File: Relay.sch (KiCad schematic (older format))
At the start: 0 parts

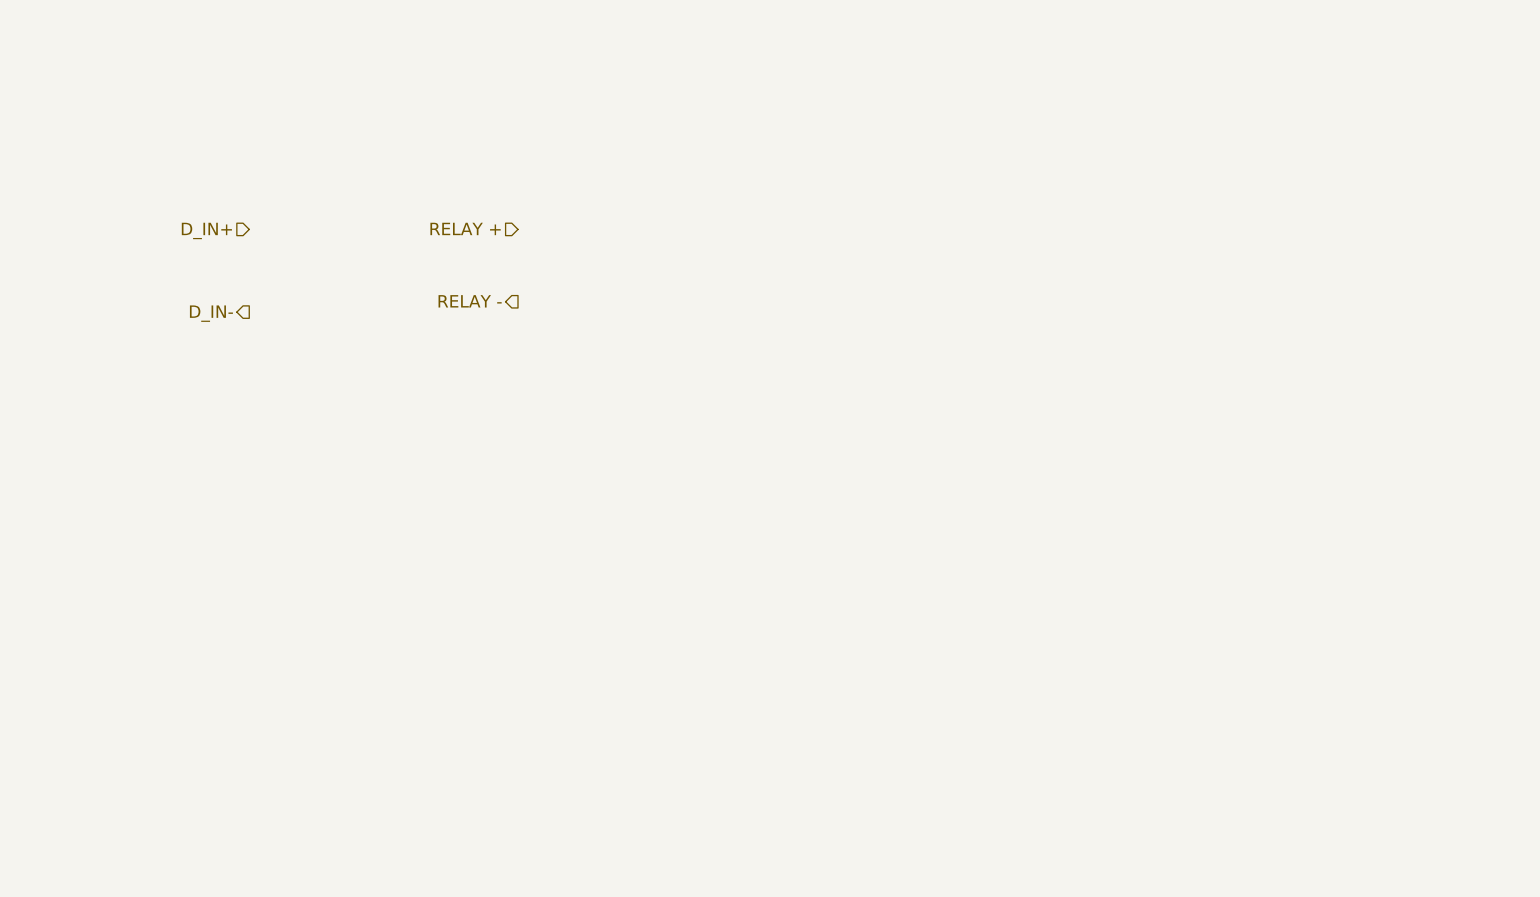
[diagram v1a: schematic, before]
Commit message: Added Relay and Fan subsystem block diagrams
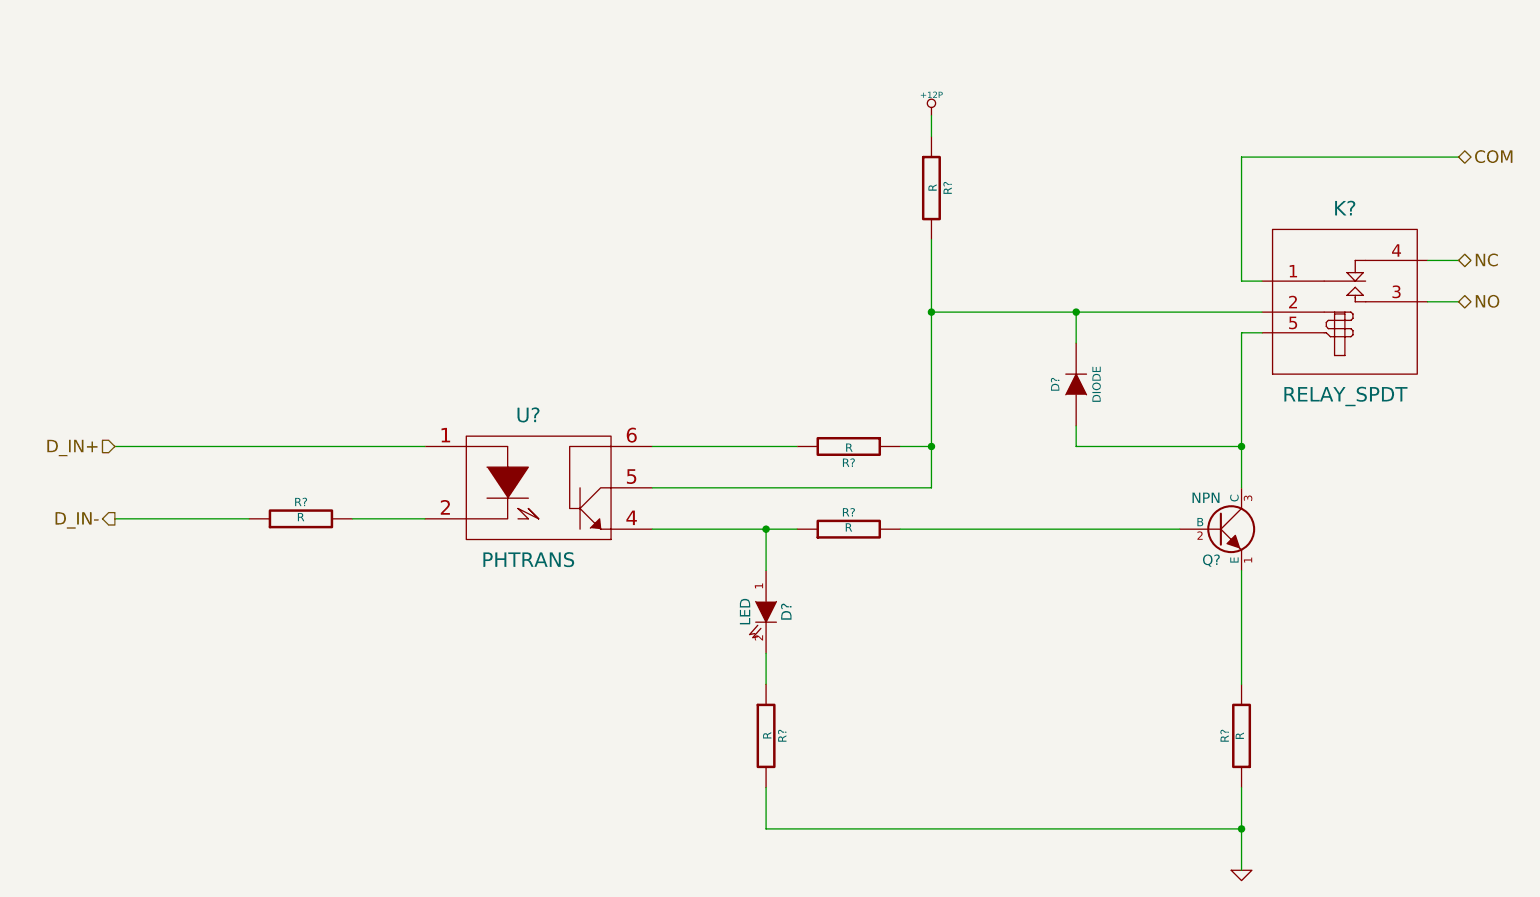
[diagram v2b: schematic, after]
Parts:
- added D?: LED, ~, symbol LED
- added D?: DIODE, ~, symbol DIODE
- added K?: RELAY_SPDT, ~, symbol RELAY_SPDT
- added Q?: NPN, ~, symbol NPN
- added R? (x6): R, ~, symbol R
- added U?: PHTRANS, ~, symbol PHTRANS
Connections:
- net D_IN+: now also U?.1
- net D_IN-: now also R?.1
- new net: R?.2, U?.2
- new net: D?.1 (A), R?.1, U?.4
- new net: D?.2 (K), K?.2 (COIL+), R?.1, R?.2, U?.5
- new net: R?.2, U?.6
- new net: Q?.1 (E), R?.2
- new net: Q?.2 (B), R?.2
- new net: D?.1 (A), K?.5 (COIL-), Q?.3 (C)
- new net: D?.2 (K), R?.1
- new net +12P: R?.1
- new net COM: K?.1 (COM)
- new net GND: R?.1, R?.2
- new net NC: K?.4 (NC)
- new net NO: K?.3 (NO)
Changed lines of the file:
@@
 LIBS:contrib
 LIBS:valves
+LIBS:CE_BenchBuddEE
 LIBS:CE_BenchBuddEE-cache
 EELAYER 27 0
@@
 $Descr A4 11693 8268
 encoding utf-8
-Sheet 7 8
+Sheet 6 8
 Title ""
-Date "4 feb 2014"
+Date "5 feb 2014"
 Rev ""
 Comp ""
@@
 Comment4 ""
 $EndDescr
-Text HLabel 3000 2650 0    60   Input ~ 0
+Text HLabel 2350 3700 0    60   Input ~ 0
 D_IN+
-Text HLabel 3000 3050 0    60   Output ~ 0
+Text HLabel 2350 4050 0    60   Output ~ 0
 D_IN-
-Text HLabel 4300 2650 0    60   Input ~ 0
-RELAY +
-Text HLabel 4300 3000 0    60   Output ~ 0
-RELAY -
+Text HLabel 8850 2800 2    60   BiDi ~ 0
+NC
+Text HLabel 8850 3000 2    60   BiDi ~ 0
+NO
+$Comp
+L PHTRANS U?
+U 1 1 52F2AFC1
+P 4400 3900
+F 0 "U?" H 4350 4250 70  0000 C CNN
+F 1 "PHTRANS" H 4350 3550 70  0000 C CNN
+F 2 "~" H 4400 3900 60  0000 C CNN
+F 3 "~" H 4400 3900 60  0000 C CNN
+	1    4400 3900
+	1    0    0    -1
+$EndComp
+$Comp
+L R R?
+U 1 1 52F2AFD0
+P 6300 2450
+F 0 "R?" V 6380 2450 40  0000 C CNN
+F 1 "R" V 6307 2451 40  0000 C CNN
+F 2 "~" V 6230 2450 30  0000 C CNN
+F 3 "~" H 6300 2450 30  0000 C CNN
+	1    6300 2450
+	1    0    0    -1
+$EndComp
+$Comp
+L NPN Q?
+U 1 1 52F2AFDF
+P 7700 4100
+F 0 "Q?" H 7700 3950 50  0000 R CNN
+F 1 "NPN" H 7700 4250 50  0000 R CNN
+F 2 "~" H 7700 4100 60  0000 C CNN
+F 3 "~" H 7700 4100 60  0000 C CNN
+	1    7700 4100
+	1    0    0    -1
+$EndComp
+$Comp
+L LED D?
+U 1 1 52F2AFEE
+P 5500 4500
+F 0 "D?" H 5500 4600 50  0000 C CNN
+F 1 "LED" H 5500 4400 50  0000 C CNN
+F 2 "~" H 5500 4500 60  0000 C CNN
+F 3 "~" H 5500 4500 60  0000 C CNN
+	1    5500 4500
+	0    1    1    0
+$EndComp
+$Comp
+L RELAY_SPDT K?
+U 1 1 52F2C7E8
+P 8300 3000
+F 0 "K?" H 8300 3450 70  0000 C CNN
+F 1 "RELAY_SPDT" H 8300 2550 70  0000 C CNN
+F 2 "~" H 8300 3000 60  0000 C CNN
+F 3 "~" H 8300 3000 60  0000 C CNN
+	1    8300 3000
+	1    0    0    -1
+$EndComp
+Text HLabel 8850 2300 2    60   BiDi ~ 0
+COM
+Wire Wire Line
+	8850 2800 8700 2800
+Wire Wire Line
+	8850 3000 8700 3000
+$Comp
+L R R?
+U 1 1 52F2C854
+P 5900 4100
+F 0 "R?" V 5980 4100 40  0000 C CNN
+F 1 "R" V 5907 4101 40  0000 C CNN
+F 2 "~" V 5830 4100 30  0000 C CNN
+F 3 "~" H 5900 4100 30  0000 C CNN
+	1    5900 4100
+	0    -1   -1   0
+$EndComp
+Wire Wire Line
+	4950 4100 5500 4100
+Wire Wire Line
+	5500 4100 5650 4100
+Wire Wire Line
+	6150 4100 7500 4100
+$Comp
+L R R?
+U 1 1 52F2C889
+P 7800 5100
+F 0 "R?" V 7880 5100 40  0000 C CNN
+F 1 "R" V 7807 5101 40  0000 C CNN
+F 2 "~" V 7730 5100 30  0000 C CNN
+F 3 "~" H 7800 5100 30  0000 C CNN
+	1    7800 5100
+	-1   0    0    1
+$EndComp
+Wire Wire Line
+	7800 4300 7800 4850
+$Comp
+L GND #PWR?
+U 1 1 52F2C8A3
+P 7800 5750
+F 0 "#PWR?" H 7800 5750 30  0001 C CNN
+F 1 "GND" H 7800 5680 30  0001 C CNN
+F 2 "" H 7800 5750 60  0000 C CNN
+F 3 "" H 7800 5750 60  0000 C CNN
+	1    7800 5750
+	1    0    0    -1
+$EndComp
+Wire Wire Line
+	5500 4100 5500 4300
+Connection ~ 5500 4100
+$Comp
+L R R?
+U 1 1 52F2C8D7
+P 5500 5100
+F 0 "R?" V 5580 5100 40  0000 C CNN
+F 1 "R" V 5507 5101 40  0000 C CNN
+F 2 "~" V 5430 5100 30  0000 C CNN
+F 3 "~" H 5500 5100 30  0000 C CNN
+	1    5500 5100
+	1    0    0    -1
+$EndComp
+Wire Wire Line
+	5500 4700 5500 4850
+Wire Wire Line
+	6300 2700 6300 3050
+Wire Wire Line
+	6300 3050 6300 3700
+Wire Wire Line
+	6300 3700 6300 3900
+$Comp
+L +12P #PWR?
+U 1 1 52F2C90E
+P 6300 2100
+F 0 "#PWR?" H 6300 2070 30  0001 C CNN
+F 1 "+12P" H 6300 2200 30  0000 C CNN
+F 2 "" H 6300 2100 60  0000 C CNN
+F 3 "" H 6300 2100 60  0000 C CNN
+	1    6300 2100
+	1    0    0    -1
+$EndComp
+Wire Wire Line
+	6300 2200 6300 2100
+Wire Wire Line
+	5500 5350 5500 5550
+Wire Wire Line
+	5500 5550 7800 5550
+$Comp
+L R R?
+U 1 1 52F2C93C
+P 3250 4050
+F 0 "R?" V 3330 4050 40  0000 C CNN
+F 1 "R" V 3257 4051 40  0000 C CNN
+F 2 "~" V 3180 4050 30  0000 C CNN
+F 3 "~" H 3250 4050 30  0000 C CNN
+	1    3250 4050
+	0    -1   -1   0
+$EndComp
+Wire Wire Line
+	3500 4050 3850 4050
+Wire Wire Line
+	3000 4050 2350 4050
+Wire Wire Line
+	2350 3700 3850 3700
+Wire Wire Line
+	6300 3900 4950 3900
+$Comp
+L R R?
+U 1 1 52F2C9AE
+P 5900 3700
+F 0 "R?" V 5980 3700 40  0000 C CNN
+F 1 "R" V 5907 3701 40  0000 C CNN
+F 2 "~" V 5830 3700 30  0000 C CNN
+F 3 "~" H 5900 3700 30  0000 C CNN
+	1    5900 3700
+	0    1    1    0
+$EndComp
+Wire Wire Line
+	4950 3700 5650 3700
+Wire Wire Line
+	6150 3700 6300 3700
+Connection ~ 6300 3700
+Wire Wire Line
+	7900 2900 7800 2900
+Wire Wire Line
+	7800 2900 7800 2300
+Wire Wire Line
+	7800 2300 8850 2300
+Wire Wire Line
+	6300 3050 7000 3050
+Wire Wire Line
+	7000 3050 7900 3050
+Connection ~ 6300 3050
+Wire Wire Line
+	7800 3150 7800 3700
+Wire Wire Line
+	7800 3700 7800 3900
+Wire Wire Line
+	7800 3150 7900 3150
+$Comp
+L DIODE D?
+U 1 1 52F2CA74
+P 7000 3400
+F 0 "D?" H 7000 3500 40  0000 C CNN
+F 1 "DIODE" H 7000 3300 40  0000 C CNN
+F 2 "~" H 7000 3400 60  0000 C CNN
+F 3 "~" H 7000 3400 60  0000 C CNN
+	1    7000 3400
+	0    -1   -1   0
+$EndComp
+Wire Wire Line
+	7800 3700 7000 3700
+Wire Wire Line
+	7000 3700 7000 3600
+Connection ~ 7800 3700
+Wire Wire Line
+	7000 3200 7000 3050
+Connection ~ 7000 3050
+Wire Wire Line
+	7800 5350 7800 5550
+Wire Wire Line
+	7800 5550 7800 5750
+Connection ~ 7800 5550
 $EndSCHEMATC

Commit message: Blocked out the LED Driver and Power sheets
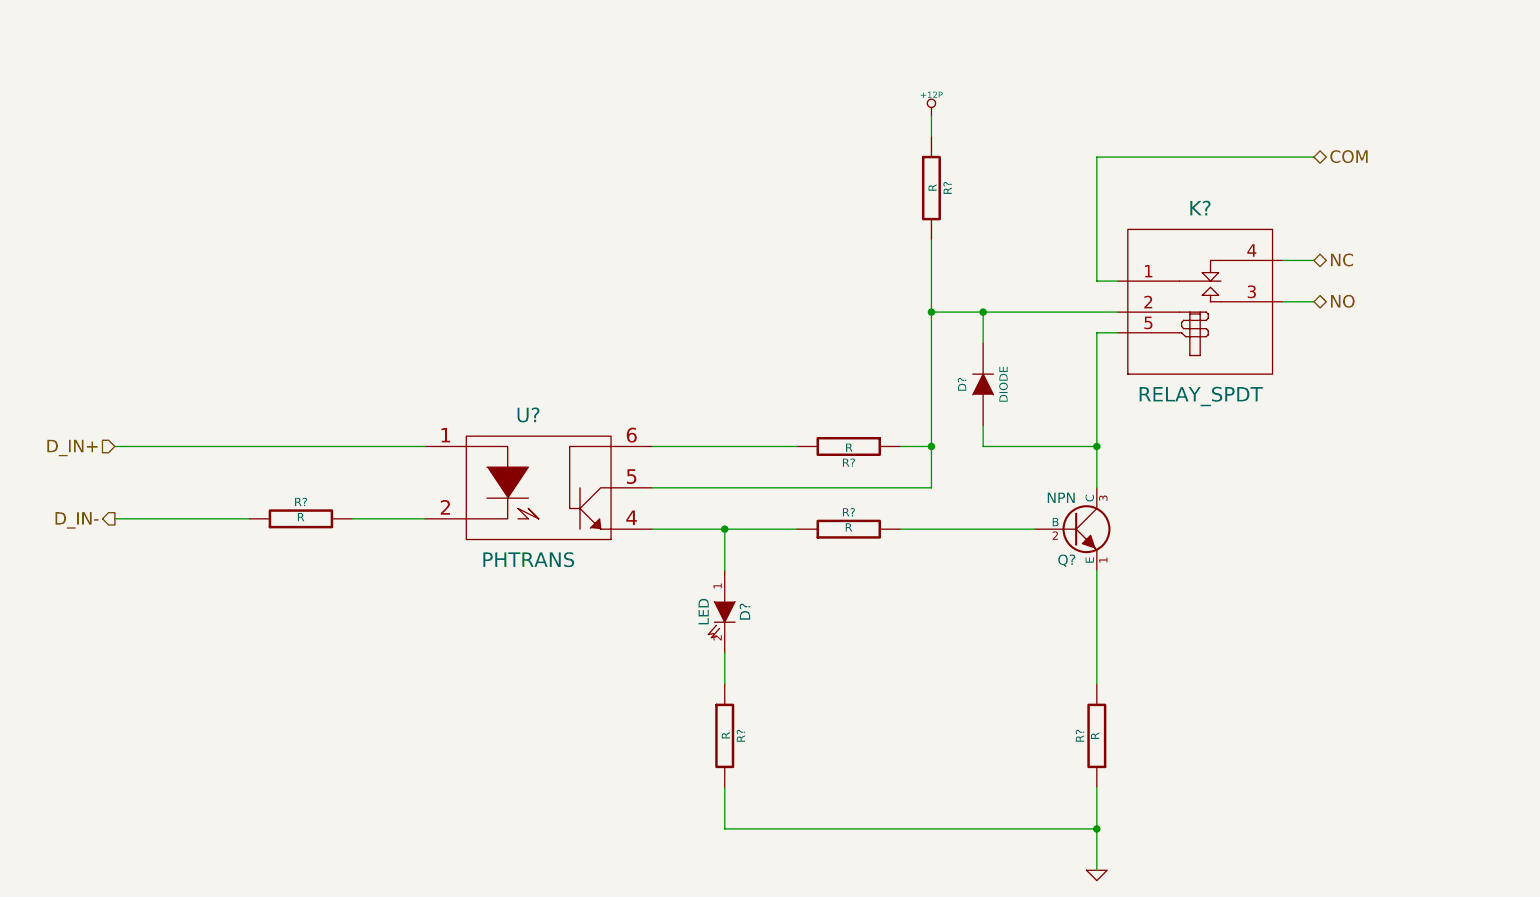
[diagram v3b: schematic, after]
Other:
- moved on the sheet: D?, K?, Q?, R?
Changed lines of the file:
@@
 LIBS:contrib
 LIBS:valves
+LIBS:CE_BenchBuddEE-cache
 LIBS:CE_BenchBuddEE
 LIBS:CE_BenchBuddEE-cache
@@
 $Descr A4 11693 8268
 encoding utf-8
-Sheet 6 8
+Sheet 4 9
 Title ""
-Date "5 feb 2014"
+Date "6 feb 2014"
 Rev ""
 Comp ""
@@
 Text HLabel 2350 4050 0    60   Output ~ 0
 D_IN-
-Text HLabel 8850 2800 2    60   BiDi ~ 0
+Text HLabel 8150 2800 2    60   BiDi ~ 0
 NC
-Text HLabel 8850 3000 2    60   BiDi ~ 0
+Text HLabel 8150 3000 2    60   BiDi ~ 0
 NO
 $Comp
@@
 L NPN Q?
 U 1 1 52F2AFDF
-P 7700 4100
-F 0 "Q?" H 7700 3950 50  0000 R CNN
-F 1 "NPN" H 7700 4250 50  0000 R CNN
-F 2 "~" H 7700 4100 60  0000 C CNN
-F 3 "~" H 7700 4100 60  0000 C CNN
-	1    7700 4100
+P 7000 4100
+F 0 "Q?" H 7000 3950 50  0000 R CNN
+F 1 "NPN" H 7000 4250 50  0000 R CNN
+F 2 "~" H 7000 4100 60  0000 C CNN
+F 3 "~" H 7000 4100 60  0000 C CNN
+	1    7000 4100
 	1    0    0    -1
 $EndComp
@@
 L LED D?
 U 1 1 52F2AFEE
-P 5500 4500
-F 0 "D?" H 5500 4600 50  0000 C CNN
-F 1 "LED" H 5500 4400 50  0000 C CNN
-F 2 "~" H 5500 4500 60  0000 C CNN
-F 3 "~" H 5500 4500 60  0000 C CNN
-	1    5500 4500
+P 5300 4500
+F 0 "D?" H 5300 4600 50  0000 C CNN
+F 1 "LED" H 5300 4400 50  0000 C CNN
+F 2 "~" H 5300 4500 60  0000 C CNN
+F 3 "~" H 5300 4500 60  0000 C CNN
+	1    5300 4500
 	0    1    1    0
 $EndComp
@@
 L RELAY_SPDT K?
 U 1 1 52F2C7E8
-P 8300 3000
-F 0 "K?" H 8300 3450 70  0000 C CNN
-F 1 "RELAY_SPDT" H 8300 2550 70  0000 C CNN
-F 2 "~" H 8300 3000 60  0000 C CNN
-F 3 "~" H 8300 3000 60  0000 C CNN
-	1    8300 3000
-	1    0    0    -1
-$EndComp
-Text HLabel 8850 2300 2    60   BiDi ~ 0
+P 7600 3000
+F 0 "K?" H 7600 3450 70  0000 C CNN
+F 1 "RELAY_SPDT" H 7600 2550 70  0000 C CNN
+F 2 "~" H 7600 3000 60  0000 C CNN
+F 3 "~" H 7600 3000 60  0000 C CNN
+	1    7600 3000
+	1    0    0    -1
+$EndComp
+Text HLabel 8150 2300 2    60   BiDi ~ 0
 COM
 Wire Wire Line
-	8850 2800 8700 2800
-Wire Wire Line
-	8850 3000 8700 3000
+	8150 2800 8000 2800
+Wire Wire Line
+	8150 3000 8000 3000
 $Comp
 L R R?
@@
 $EndComp
 Wire Wire Line
-	4950 4100 5500 4100
-Wire Wire Line
-	5500 4100 5650 4100
-Wire Wire Line
-	6150 4100 7500 4100
+	4950 4100 5300 4100
+Wire Wire Line
+	5300 4100 5650 4100
+Wire Wire Line
+	6150 4100 6800 4100
 $Comp
 L R R?
 U 1 1 52F2C889
-P 7800 5100
-F 0 "R?" V 7880 5100 40  0000 C CNN
-F 1 "R" V 7807 5101 40  0000 C CNN
-F 2 "~" V 7730 5100 30  0000 C CNN
-F 3 "~" H 7800 5100 30  0000 C CNN
-	1    7800 5100
+P 7100 5100
+F 0 "R?" V 7180 5100 40  0000 C CNN
+F 1 "R" V 7107 5101 40  0000 C CNN
+F 2 "~" V 7030 5100 30  0000 C CNN
+F 3 "~" H 7100 5100 30  0000 C CNN
+	1    7100 5100
 	-1   0    0    1
 $EndComp
 Wire Wire Line
-	7800 4300 7800 4850
+	7100 4300 7100 4850
 $Comp
 L GND #PWR?
 U 1 1 52F2C8A3
-P 7800 5750
-F 0 "#PWR?" H 7800 5750 30  0001 C CNN
-F 1 "GND" H 7800 5680 30  0001 C CNN
-F 2 "" H 7800 5750 60  0000 C CNN
-F 3 "" H 7800 5750 60  0000 C CNN
-	1    7800 5750
-	1    0    0    -1
-$EndComp
-Wire Wire Line
-	5500 4100 5500 4300
-Connection ~ 5500 4100
+P 7100 5750
+F 0 "#PWR?" H 7100 5750 30  0001 C CNN
+F 1 "GND" H 7100 5680 30  0001 C CNN
+F 2 "" H 7100 5750 60  0000 C CNN
+F 3 "" H 7100 5750 60  0000 C CNN
+	1    7100 5750
+	1    0    0    -1
+$EndComp
 $Comp
 L R R?
 U 1 1 52F2C8D7
-P 5500 5100
-F 0 "R?" V 5580 5100 40  0000 C CNN
-F 1 "R" V 5507 5101 40  0000 C CNN
-F 2 "~" V 5430 5100 30  0000 C CNN
-F 3 "~" H 5500 5100 30  0000 C CNN
-	1    5500 5100
-	1    0    0    -1
-$EndComp
-Wire Wire Line
-	5500 4700 5500 4850
+P 5300 5100
+F 0 "R?" V 5380 5100 40  0000 C CNN
+F 1 "R" V 5307 5101 40  0000 C CNN
+F 2 "~" V 5230 5100 30  0000 C CNN
+F 3 "~" H 5300 5100 30  0000 C CNN
+	1    5300 5100
+	1    0    0    -1
+$EndComp
+Wire Wire Line
+	5300 4700 5300 4850
 Wire Wire Line
 	6300 2700 6300 3050
@@
 	6300 2200 6300 2100
 Wire Wire Line
-	5500 5350 5500 5550
-Wire Wire Line
-	5500 5550 7800 5550
+	5300 5550 7100 5550
 $Comp
 L R R?
@@
 Connection ~ 6300 3700
 Wire Wire Line
-	7900 2900 7800 2900
-Wire Wire Line
-	7800 2900 7800 2300
-Wire Wire Line
-	7800 2300 8850 2300
-Wire Wire Line
-	6300 3050 7000 3050
-Wire Wire Line
-	7000 3050 7900 3050
+	7200 2900 7100 2900
+Wire Wire Line
+	7100 2900 7100 2300
+Wire Wire Line
+	7100 2300 8150 2300
+Wire Wire Line
+	6300 3050 6550 3050
+Wire Wire Line
+	6550 3050 7200 3050
 Connection ~ 6300 3050
 Wire Wire Line
-	7800 3150 7800 3700
-Wire Wire Line
-	7800 3700 7800 3900
-Wire Wire Line
-	7800 3150 7900 3150
+	7100 3150 7100 3700
+Wire Wire Line
+	7100 3700 7100 3900
+Wire Wire Line
+	7100 3150 7200 3150
 $Comp
 L DIODE D?
 U 1 1 52F2CA74
-P 7000 3400
-F 0 "D?" H 7000 3500 40  0000 C CNN
-F 1 "DIODE" H 7000 3300 40  0000 C CNN
-F 2 "~" H 7000 3400 60  0000 C CNN
-F 3 "~" H 7000 3400 60  0000 C CNN
-	1    7000 3400
+P 6550 3400
+F 0 "D?" H 6550 3500 40  0000 C CNN
+F 1 "DIODE" H 6550 3300 40  0000 C CNN
+F 2 "~" H 6550 3400 60  0000 C CNN
+F 3 "~" H 6550 3400 60  0000 C CNN
+	1    6550 3400
 	0    -1   -1   0
 $EndComp
 Wire Wire Line
-	7800 3700 7000 3700
-Wire Wire Line
-	7000 3700 7000 3600
-Connection ~ 7800 3700
-Wire Wire Line
-	7000 3200 7000 3050
-Connection ~ 7000 3050
-Wire Wire Line
-	7800 5350 7800 5550
-Wire Wire Line
-	7800 5550 7800 5750
-Connection ~ 7800 5550
+	7100 3700 6550 3700
+Wire Wire Line
+	6550 3700 6550 3600
+Connection ~ 7100 3700
+Wire Wire Line
+	6550 3200 6550 3050
+Connection ~ 6550 3050
+Wire Wire Line
+	7100 5350 7100 5550
+Wire Wire Line
+	7100 5550 7100 5750
+Connection ~ 7100 5550
+Wire Wire Line
+	5300 4300 5300 4100
+Connection ~ 5300 4100
+Wire Wire Line
+	5300 5550 5300 5350
 $EndSCHEMATC
